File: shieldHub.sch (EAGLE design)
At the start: 11 parts

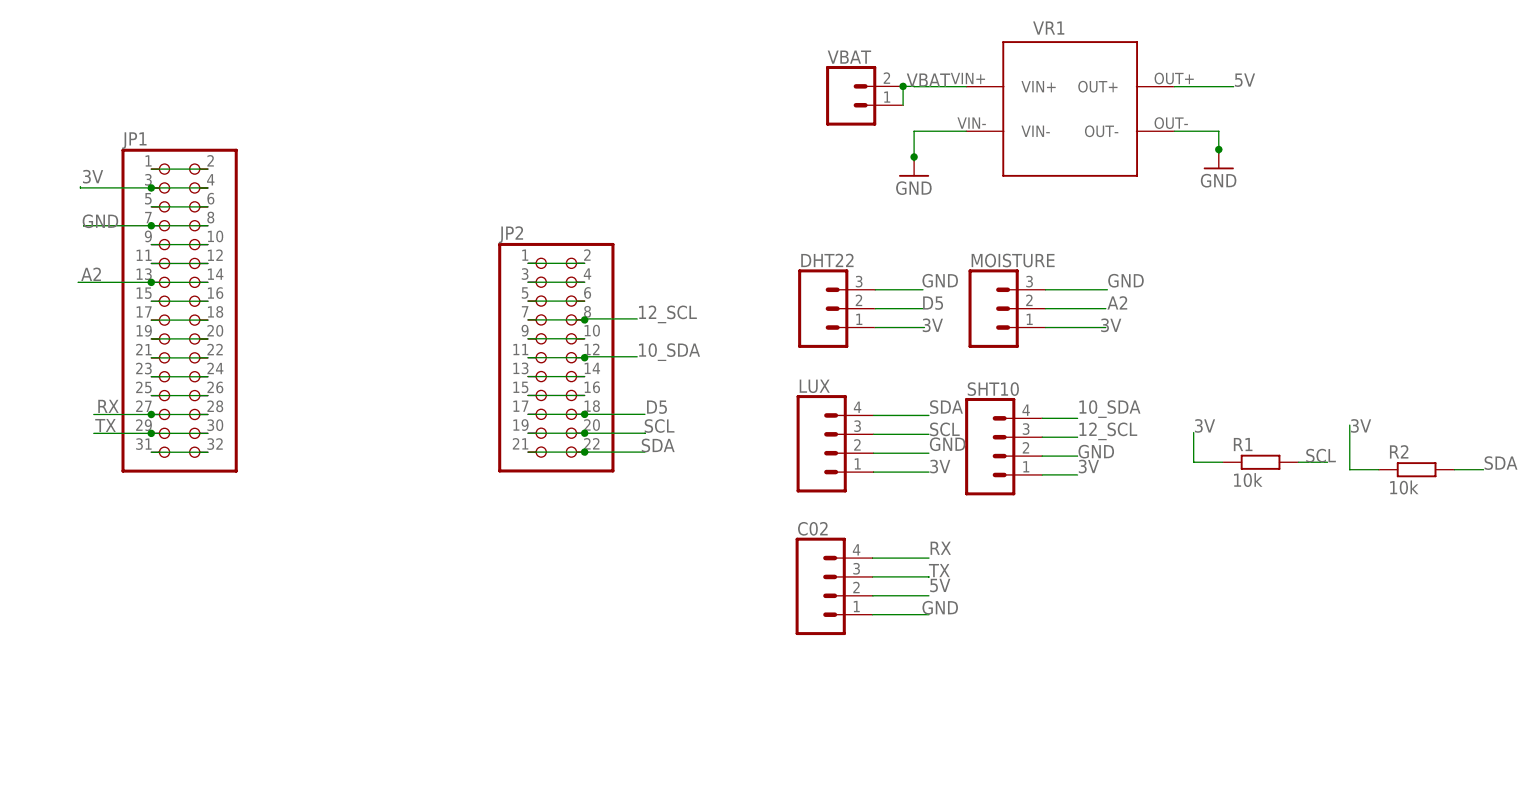
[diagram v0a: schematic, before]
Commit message: Removes sensor connector pins and adds rrm69 header pin
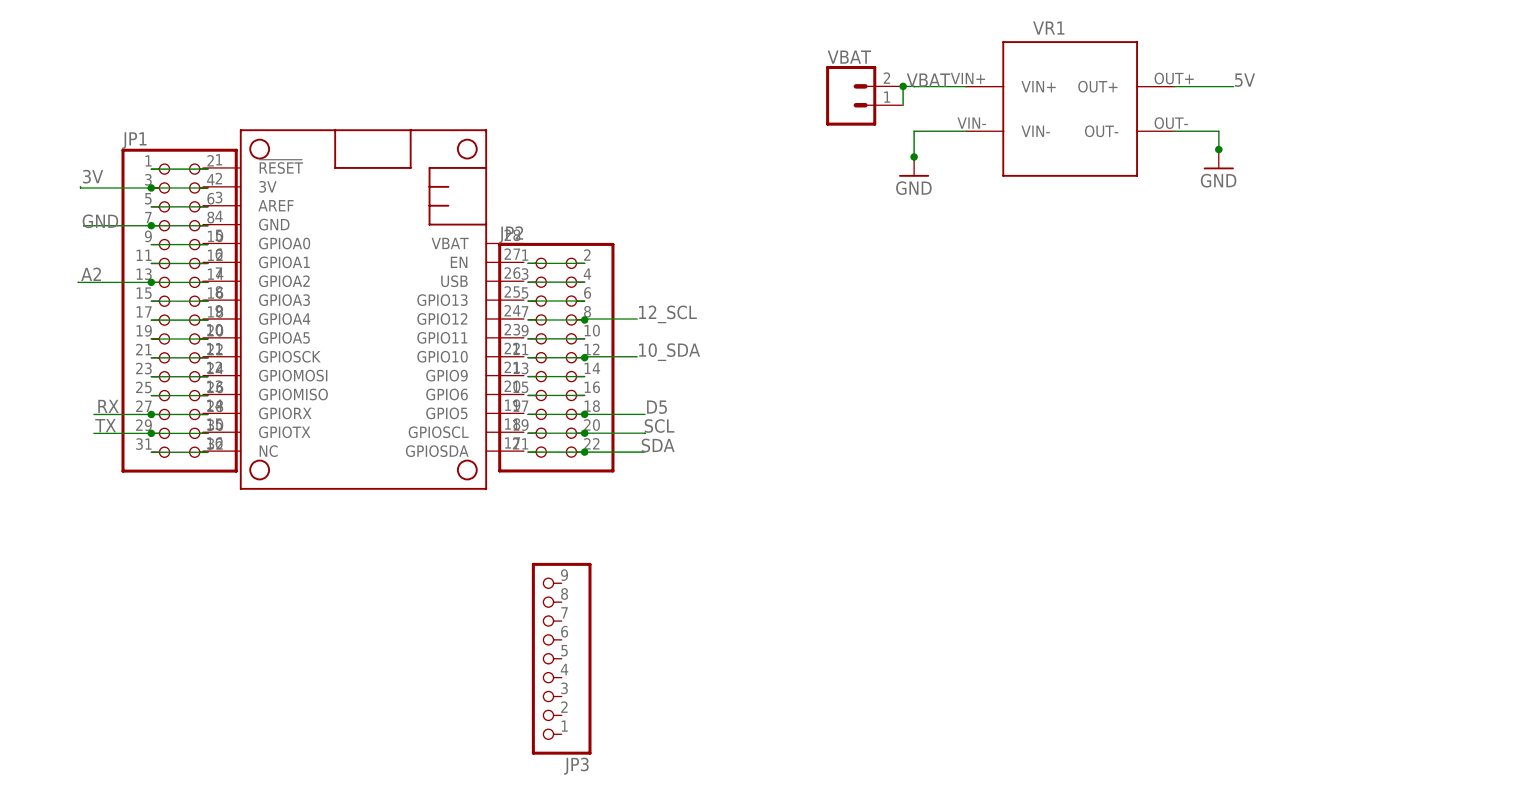
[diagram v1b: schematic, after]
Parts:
- removed C02, LUX, SHT10: (no value), SparkFun-Connectors:CONN_04SCREW
- removed DHT22, MOISTURE: (no value), SparkFun-Connectors:CONN_03SCREW
- removed R1, R2: 10k, resistor:R-EU_0207/10
- added JP3: (no value), adafruit:PINHD-1X9
- added MS1: FEATHERWING, adafruit:FEATHERWING
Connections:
- net 10_SDA: no longer SHT10.4
- net 12_SCL: no longer SHT10.3
- net 3V: no longer DHT22.1, LUX.1, MOISTURE.1, R1.1, R2.1, SHT10.1
- net 5V: no longer C02.2
- net A2: no longer MOISTURE.2
- net D5: no longer DHT22.2
- net GND: no longer C02.1, DHT22.3, LUX.2, MOISTURE.3, SHT10.2
- net RX: no longer C02.4
- net SCL: no longer LUX.3, R1.2
- net SDA: no longer LUX.4, R2.2
- net TX: no longer C02.3
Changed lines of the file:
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@@
 <part name="JP2" library="pinhead" library_urn="urn:adsk.eagle:library:325" deviceset="PINHD-2X11" device="" package3d_urn="urn:adsk.eagle:package:22419/2"/>
 <part name="VR1" library="lm2577_module" deviceset="MT3608" device="THROUGH_HOLE"/>
-<part name="R1" library="resistor" library_urn="urn:adsk.eagle:library:348" deviceset="R-EU_" device="0207/10" package3d_urn="urn:adsk.eagle:package:25939/1" value="10k"/>
-<part name="R2" library="resistor" library_urn="urn:adsk.eagle:library:348" deviceset="R-EU_" device="0207/10" package3d_urn="urn:adsk.eagle:package:25939/1" value="10k"/>
-<part name="DHT22" library="SparkFun-Connectors" deviceset="CONN_03" device="SCREW"/>
-<part name="MOISTURE" library="SparkFun-Connectors" deviceset="CONN_03" device="SCREW"/>
-<part name="LUX" library="SparkFun-Connectors" deviceset="CONN_04" device="SCREW"/>
-<part name="SHT10" library="SparkFun-Connectors" deviceset="CONN_04" device="SCREW"/>
-<part name="C02" library="SparkFun-Connectors" deviceset="CONN_04" device="SCREW"/>
 <part name="VBAT" library="SparkFun-Connectors" deviceset="CONN_02" device=""/>
 <part name="GND1" library="supply1" library_urn="urn:adsk.eagle:library:371" deviceset="GND" device=""/>
 <part name="GND2" library="supply1" library_urn="urn:adsk.eagle:library:371" deviceset="GND" device=""/>
+<part name="MS1" library="adafruit" deviceset="FEATHERWING" device=""/>
+<part name="JP3" library="adafruit" deviceset="PINHD-1X9" device=""/>
 </parts>
 <sheets>
@@
 <attribute name="VALUE" x="132" y="95" size="1.778" layer="96"/>
 </instance>
-<instance part="R1" gate="G$1" x="162.62" y="59.46" smashed="yes">
-<attribute name="NAME" x="158.81" y="60.9586" size="1.778" layer="95"/>
-<attribute name="VALUE" x="158.81" y="56.158" size="1.778" layer="96"/>
-</instance>
-<instance part="R2" gate="G$1" x="183.62" y="58.46" smashed="yes">
-<attribute name="NAME" x="179.81" y="59.9586" size="1.778" layer="95"/>
-<attribute name="VALUE" x="179.81" y="55.158" size="1.778" layer="96"/>
-</instance>
-<instance part="DHT22" gate="J$1" x="103.14" y="80.13" smashed="yes">
-<attribute name="VALUE" x="100.6" y="72.764" size="1.778" layer="96" font="vector"/>
-<attribute name="NAME" x="100.6" y="85.718" size="1.778" layer="95" font="vector"/>
-</instance>
-<instance part="MOISTURE" gate="J$1" x="126.07" y="80.13" smashed="yes">
-<attribute name="VALUE" x="123.53" y="72.764" size="1.778" layer="96" font="vector"/>
-<attribute name="NAME" x="123.53" y="85.718" size="1.778" layer="95" font="vector"/>
-</instance>
-<instance part="LUX" gate="G$1" x="105.47" y="60.68" smashed="yes">
-<attribute name="VALUE" x="100.39" y="53.314" size="1.778" layer="96" font="vector"/>
-<attribute name="NAME" x="100.39" y="68.808" size="1.778" layer="95" font="vector"/>
-</instance>
-<instance part="SHT10" gate="G$1" x="128.15" y="60.29" smashed="yes">
-<attribute name="VALUE" x="123.07" y="52.924" size="1.778" layer="96" font="vector"/>
-<attribute name="NAME" x="123.07" y="68.418" size="1.778" layer="95" font="vector"/>
-</instance>
-<instance part="C02" gate="G$1" x="105.34" y="41.49" smashed="yes">
-<attribute name="VALUE" x="100.26" y="34.124" size="1.778" layer="96" font="vector"/>
-<attribute name="NAME" x="100.26" y="49.618" size="1.778" layer="95" font="vector"/>
-</instance>
 <instance part="VBAT" gate="G$1" x="106.9" y="107.5" smashed="yes">
 <attribute name="VALUE" x="104.36" y="102.674" size="1.778" layer="96" font="vector"/>
@@
 <instance part="GND2" gate="1" x="157" y="99" smashed="yes">
 <attribute name="VALUE" x="154.46" y="96.46" size="1.778" layer="96"/>
+</instance>
+<instance part="MS1" gate="G$1" x="25.4" y="104.14" smashed="yes" rot="R270"/>
+<instance part="JP3" gate="G$1" x="66.04" y="33.02" smashed="yes" rot="R180">
+<attribute name="NAME" x="72.39" y="19.685" size="1.778" layer="95" rot="R180"/>
+<attribute name="VALUE" x="72.39" y="48.26" size="1.778" layer="96" rot="R180"/>
 </instance>
 </instances>
@@
 <label x="4" y="97" size="1.778" layer="95"/>
 </segment>
-<segment>
-<pinref part="DHT22" gate="J$1" pin="1"/>
-<wire x1="110.76" y1="77.59" x2="117.4" y2="77.59" width="0.1524" layer="91"/>
-<label x="117" y="77" size="1.778" layer="95"/>
-</segment>
-<segment>
-<pinref part="MOISTURE" gate="J$1" pin="1"/>
-<wire x1="133.69" y1="77.59" x2="141.8" y2="77.59" width="0.1524" layer="91"/>
-<label x="141" y="77" size="1.778" layer="95"/>
-</segment>
-<segment>
-<pinref part="LUX" gate="G$1" pin="1"/>
-<wire x1="110.55" y1="58.14" x2="118" y2="58.14" width="0.1524" layer="91"/>
-<label x="118" y="58" size="1.778" layer="95"/>
-</segment>
-<segment>
-<pinref part="SHT10" gate="G$1" pin="1"/>
-<wire x1="133.23" y1="57.75" x2="138" y2="57.75" width="0.1524" layer="91"/>
-<label x="138" y="58" size="1.778" layer="95"/>
-</segment>
-<segment>
-<pinref part="R1" gate="G$1" pin="1"/>
-<wire x1="157.54" y1="59.46" x2="153.62" y2="59.46" width="0.1524" layer="91"/>
-<wire x1="153.62" y1="59.46" x2="153.62" y2="63.46" width="0.1524" layer="91"/>
-<label x="153.62" y="63.46" size="1.778" layer="95"/>
-</segment>
-<segment>
-<pinref part="R2" gate="G$1" pin="1"/>
-<wire x1="178.54" y1="58.46" x2="174.62" y2="58.46" width="0.1524" layer="91"/>
-<wire x1="174.62" y1="58.46" x2="174.62" y2="64.46" width="0.1524" layer="91"/>
-<label x="174.62" y="63.46" size="1.778" layer="95"/>
-</segment>
 </net>
 <net name="N$3" class="0">
@@
 <junction x="157" y="101.54"/>
 </segment>
-<segment>
-<pinref part="DHT22" gate="J$1" pin="3"/>
-<wire x1="110.76" y1="82.67" x2="117.2" y2="82.67" width="0.1524" layer="91"/>
-<label x="117" y="83" size="1.778" layer="95"/>
-</segment>
-<segment>
-<pinref part="MOISTURE" gate="J$1" pin="3"/>
-<wire x1="133.69" y1="82.67" x2="142" y2="82.67" width="0.1524" layer="91"/>
-<label x="142" y="83" size="1.778" layer="95"/>
-</segment>
-<segment>
-<pinref part="LUX" gate="G$1" pin="2"/>
-<wire x1="110.55" y1="60.68" x2="118" y2="60.68" width="0.1524" layer="91"/>
-<label x="118" y="61" size="1.778" layer="95"/>
-</segment>
-<segment>
-<pinref part="SHT10" gate="G$1" pin="2"/>
-<wire x1="133.23" y1="60.29" x2="138" y2="60.29" width="0.1524" layer="91"/>
-<label x="138" y="60" size="1.778" layer="95"/>
-</segment>
-<segment>
-<pinref part="C02" gate="G$1" pin="1"/>
-<wire x1="110.42" y1="38.95" x2="118" y2="38.95" width="0.1524" layer="91"/>
-<label x="117" y="39" size="1.778" layer="95"/>
-</segment>
 </net>
 <net name="N$5" class="0">
@@
 <label x="3.91" y="83.85" size="1.778" layer="95"/>
 </segment>
-<segment>
-<pinref part="MOISTURE" gate="J$1" pin="2"/>
-<wire x1="133.69" y1="80.13" x2="141.8" y2="80.13" width="0.1524" layer="91"/>
-<label x="142" y="80" size="1.778" layer="95"/>
-</segment>
 </net>
 <net name="N$8" class="0">
@@
 <label x="6.01" y="66.09" size="1.778" layer="95"/>
 </segment>
-<segment>
-<pinref part="C02" gate="G$1" pin="4"/>
-<wire x1="110.42" y1="46.57" x2="118" y2="46.57" width="0.1524" layer="91"/>
-<label x="118" y="47" size="1.778" layer="95"/>
-</segment>
 </net>
 <net name="TX" class="0">
@@
 <label x="5.82" y="63.51" size="1.778" layer="95"/>
 </segment>
-<segment>
-<pinref part="C02" gate="G$1" pin="3"/>
-<wire x1="110.42" y1="44.03" x2="118" y2="44.03" width="0.1524" layer="91"/>
-<wire x1="118" y1="44.03" x2="118" y2="44" width="0.1524" layer="91"/>
-<label x="118" y="44" size="1.778" layer="95"/>
-</segment>
 </net>
 <net name="N$16" class="0">
@@
 <junction x="71.67" y="65.91"/>
 <label x="79.85" y="66" size="1.778" layer="95"/>
-</segment>
-<segment>
-<pinref part="DHT22" gate="J$1" pin="2"/>
-<wire x1="110.76" y1="80.13" x2="117.2" y2="80.13" width="0.1524" layer="91"/>
-<label x="117" y="80" size="1.778" layer="95"/>
 </segment>
 </net>
@@
 <label x="79.61" y="63.45" size="1.778" layer="95"/>
 </segment>
-<segment>
-<pinref part="LUX" gate="G$1" pin="3"/>
-<wire x1="110.55" y1="63.22" x2="118" y2="63.22" width="0.1524" layer="91"/>
-<label x="118" y="63" size="1.778" layer="95"/>
-</segment>
-<segment>
-<pinref part="R1" gate="G$1" pin="2"/>
-<wire x1="167.7" y1="59.46" x2="171.62" y2="59.46" width="0.1524" layer="91"/>
-<label x="168.62" y="59.46" size="1.778" layer="95"/>
-</segment>
 </net>
 <net name="SDA" class="0">
@@
 <junction x="71.67" y="60.83"/>
 <label x="79.21" y="60.83" size="1.778" layer="95"/>
-</segment>
-<segment>
-<pinref part="LUX" gate="G$1" pin="4"/>
-<wire x1="110.55" y1="65.76" x2="118" y2="65.76" width="0.1524" layer="91"/>
-<label x="118" y="66" size="1.778" layer="95"/>
-</segment>
-<segment>
-<pinref part="R2" gate="G$1" pin="2"/>
-<wire x1="188.7" y1="58.46" x2="192.62" y2="58.46" width="0.1524" layer="91"/>
-<label x="192.62" y="58.46" size="1.778" layer="95"/>
 </segment>
 </net>
@@
 <net name="5V" class="0">
 <segment>
-<pinref part="C02" gate="G$1" pin="2"/>
-<wire x1="110.42" y1="41.49" x2="118" y2="41.49" width="0.1524" layer="91"/>
-<label x="118" y="42" size="1.778" layer="95"/>
-</segment>
-<segment>
 <pinref part="VR1" gate="G$1" pin="OUT+"/>
 <wire x1="151" y1="110" x2="159" y2="110" width="0.1524" layer="91"/>
@@
 </net>
 <net name="10_SDA" class="0">
-<segment>
-<pinref part="SHT10" gate="G$1" pin="4"/>
-<wire x1="133.23" y1="65.37" x2="138" y2="65.37" width="0.1524" layer="91"/>
-<label x="138" y="66" size="1.778" layer="95"/>
-</segment>
 <segment>
 <pinref part="JP2" gate="A" pin="11"/>
@@
 <net name="12_SCL" class="0">
 <segment>
-<pinref part="SHT10" gate="G$1" pin="3"/>
-<wire x1="133.23" y1="62.83" x2="138" y2="62.83" width="0.1524" layer="91"/>
-<label x="138" y="63" size="1.778" layer="95"/>
-</segment>
-<segment>
 <pinref part="JP2" gate="A" pin="7"/>

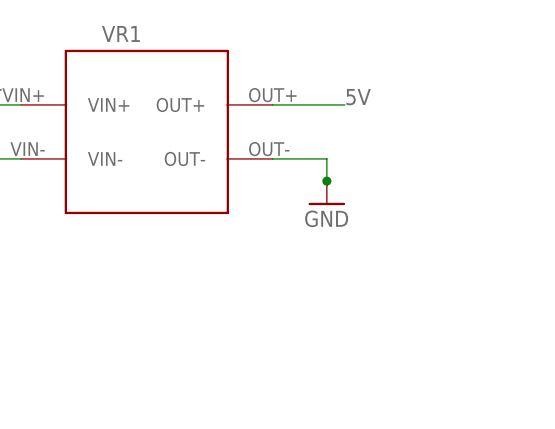
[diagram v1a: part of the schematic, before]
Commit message: Adds connector pin for fan power
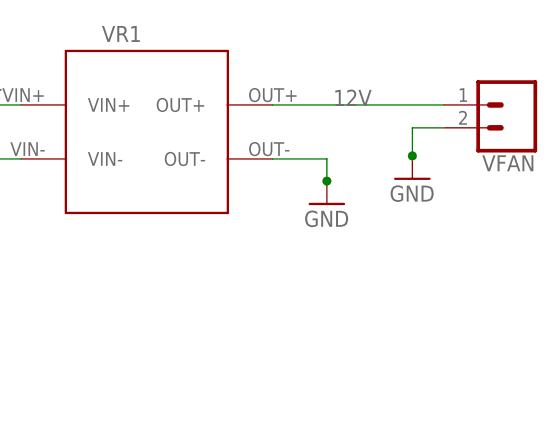
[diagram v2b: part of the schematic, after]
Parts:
- added VFAN: (no value), SparkFun-Connectors:CONN_02
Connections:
- removed net 5V: VR1.OUT+
- new net 12V: VFAN.1, VR1.OUT+
- net GND: now also VFAN.2
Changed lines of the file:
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@@
 <setting verticaltext="up"/>
 </settings>
-<grid distance="0.1" unitdist="inch" unit="inch" style="lines" multiple="1" display="no" altdistance="0.01" altunitdist="inch" altunit="inch"/>
+<grid distance="0.1" unitdist="mm" unit="mm" style="dots" multiple="1" display="yes" altdistance="1" altunitdist="mm" altunit="mm"/>
 <layers>
 <layer number="1" name="Top" color="4" fill="1" visible="no" active="no"/>
@@
 <part name="MS1" library="adafruit" deviceset="FEATHERWING" device=""/>
 <part name="JP3" library="adafruit" deviceset="PINHD-1X9" device=""/>
+<part name="VFAN" library="SparkFun-Connectors" deviceset="CONN_02" device=""/>
+<part name="GND3" library="supply1" library_urn="urn:adsk.eagle:library:371" deviceset="GND" device=""/>
 </parts>
 <sheets>
@@
 <attribute name="VALUE" x="72.39" y="48.26" size="1.778" layer="96" rot="R180"/>
 </instance>
+<instance part="VFAN" gate="G$1" x="177.62" y="110" smashed="yes" rot="R180">
+<attribute name="VALUE" x="180.16" y="114.826" size="1.778" layer="96" font="vector" rot="R180"/>
+<attribute name="NAME" x="180.16" y="104.412" size="1.778" layer="95" font="vector" rot="R180"/>
+</instance>
+<instance part="GND3" gate="1" x="166.5" y="101.8" smashed="yes">
+<attribute name="VALUE" x="163.96" y="99.26" size="1.778" layer="96"/>
+</instance>
 </instances>
 <busses>
@@
 <wire x1="157" y1="101.54" x2="157" y2="101" width="0.1524" layer="91"/>
 <junction x="157" y="101.54"/>
+</segment>
+<segment>
+<pinref part="VFAN" gate="G$1" pin="2"/>
+<wire x1="170" y1="107.46" x2="166.5" y2="107.46" width="0.1524" layer="91"/>
+<wire x1="166.5" y1="107.46" x2="166.5" y2="104.34" width="0.1524" layer="91"/>
+<wire x1="166.5" y1="104.34" x2="166.5" y2="104.2" width="0.1524" layer="91"/>
+<wire x1="166.5" y1="104.2" x2="166.4" y2="104.2" width="0.1524" layer="91"/>
+<pinref part="GND3" gate="1" pin="GND"/>
+<junction x="166.5" y="104.34"/>
 </segment>
 </net>
@@
 </segment>
 </net>
-<net name="5V" class="0">
+<net name="12V" class="0">
 <segment>
 <pinref part="VR1" gate="G$1" pin="OUT+"/>
-<wire x1="151" y1="110" x2="159" y2="110" width="0.1524" layer="91"/>
-<label x="159" y="110" size="1.778" layer="95"/>
-</segment>
-</net>
+<pinref part="VFAN" gate="G$1" pin="1"/>
+<wire x1="151" y1="110" x2="170" y2="110" width="0.1524" layer="91"/>
+<label x="157.7" y="109.9" size="1.778" layer="95"/>
+</segment>
+</net>
